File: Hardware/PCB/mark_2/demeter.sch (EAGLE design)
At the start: 70 parts, among them IC1 4050, IC2 LM1117-5.0, IC3 LM1117-3.3, IC4 M24C64, IC5 MCP3424, IC6 MCP23017SO, IC7 MAX485, IC8 ATMEGA32U4-AU, Q1 IRLML6402, Q2 IRLML6402, Q3 IRLML6402, Q4 IRLML6402, Q5 IRLML6402, Q6 IRLML6402, Q7 IRLML6402, Q8 IRLML6402

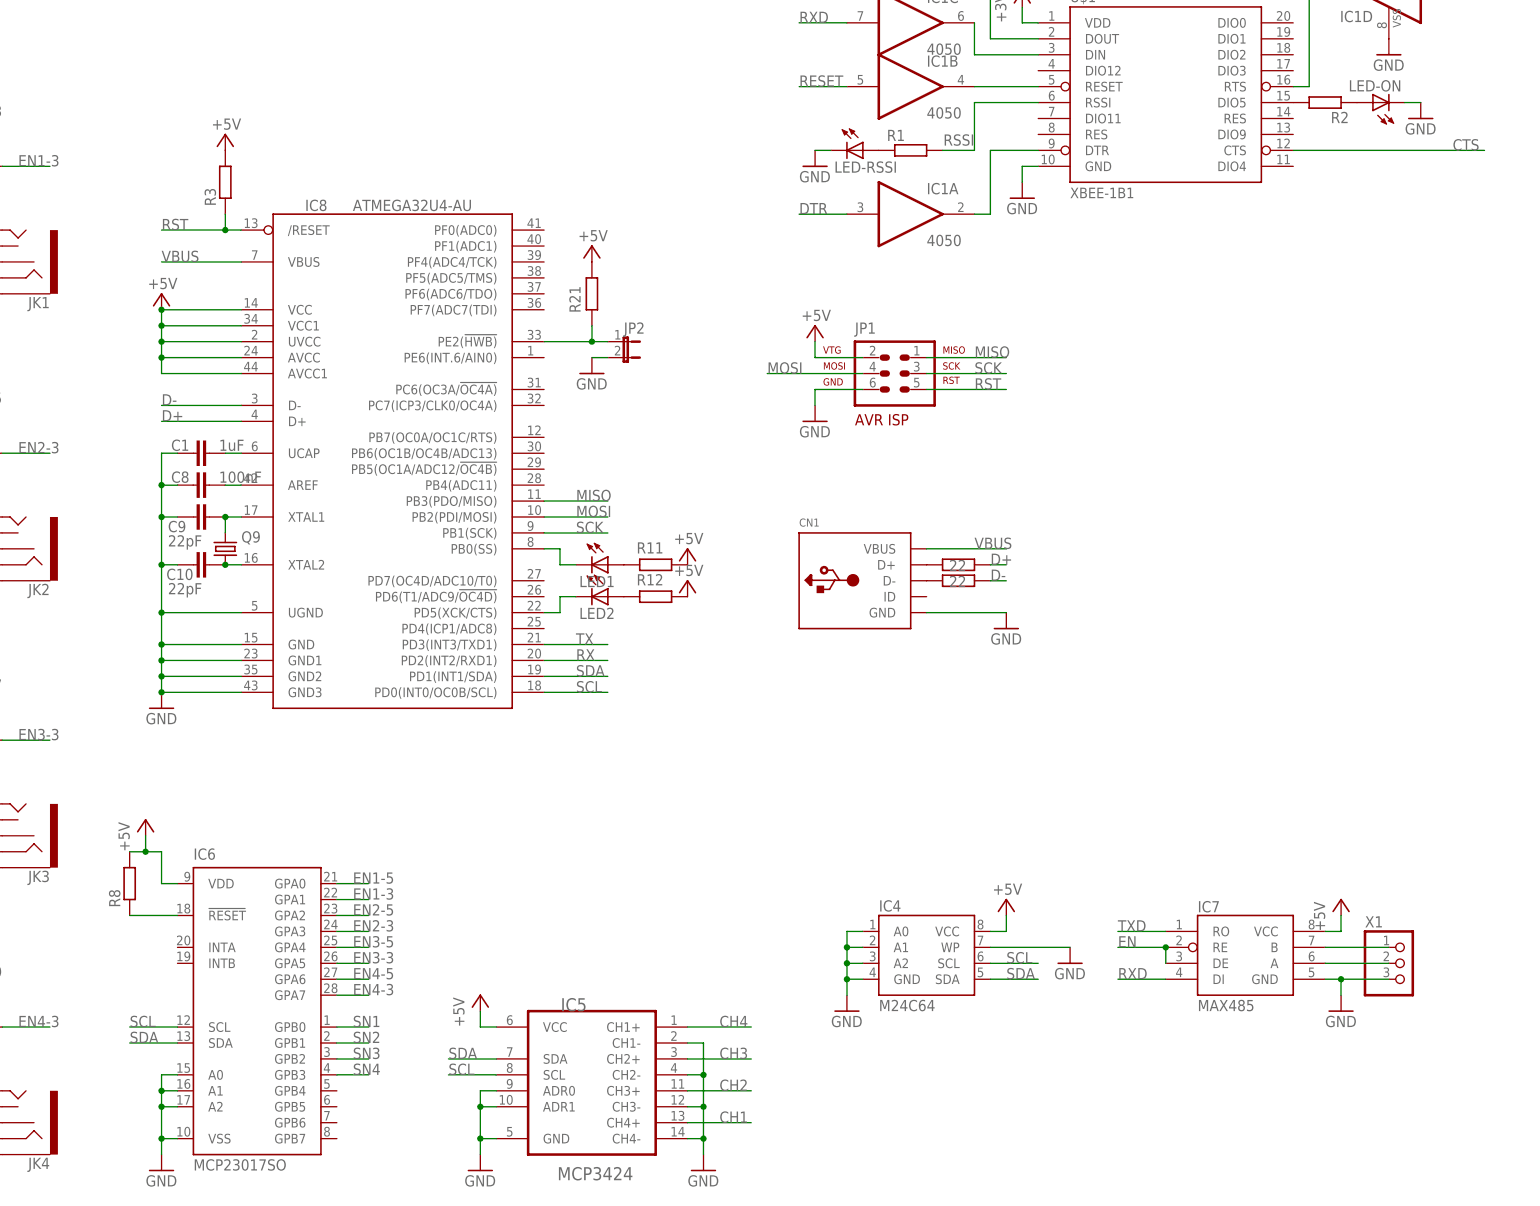
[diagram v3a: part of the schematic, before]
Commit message: 
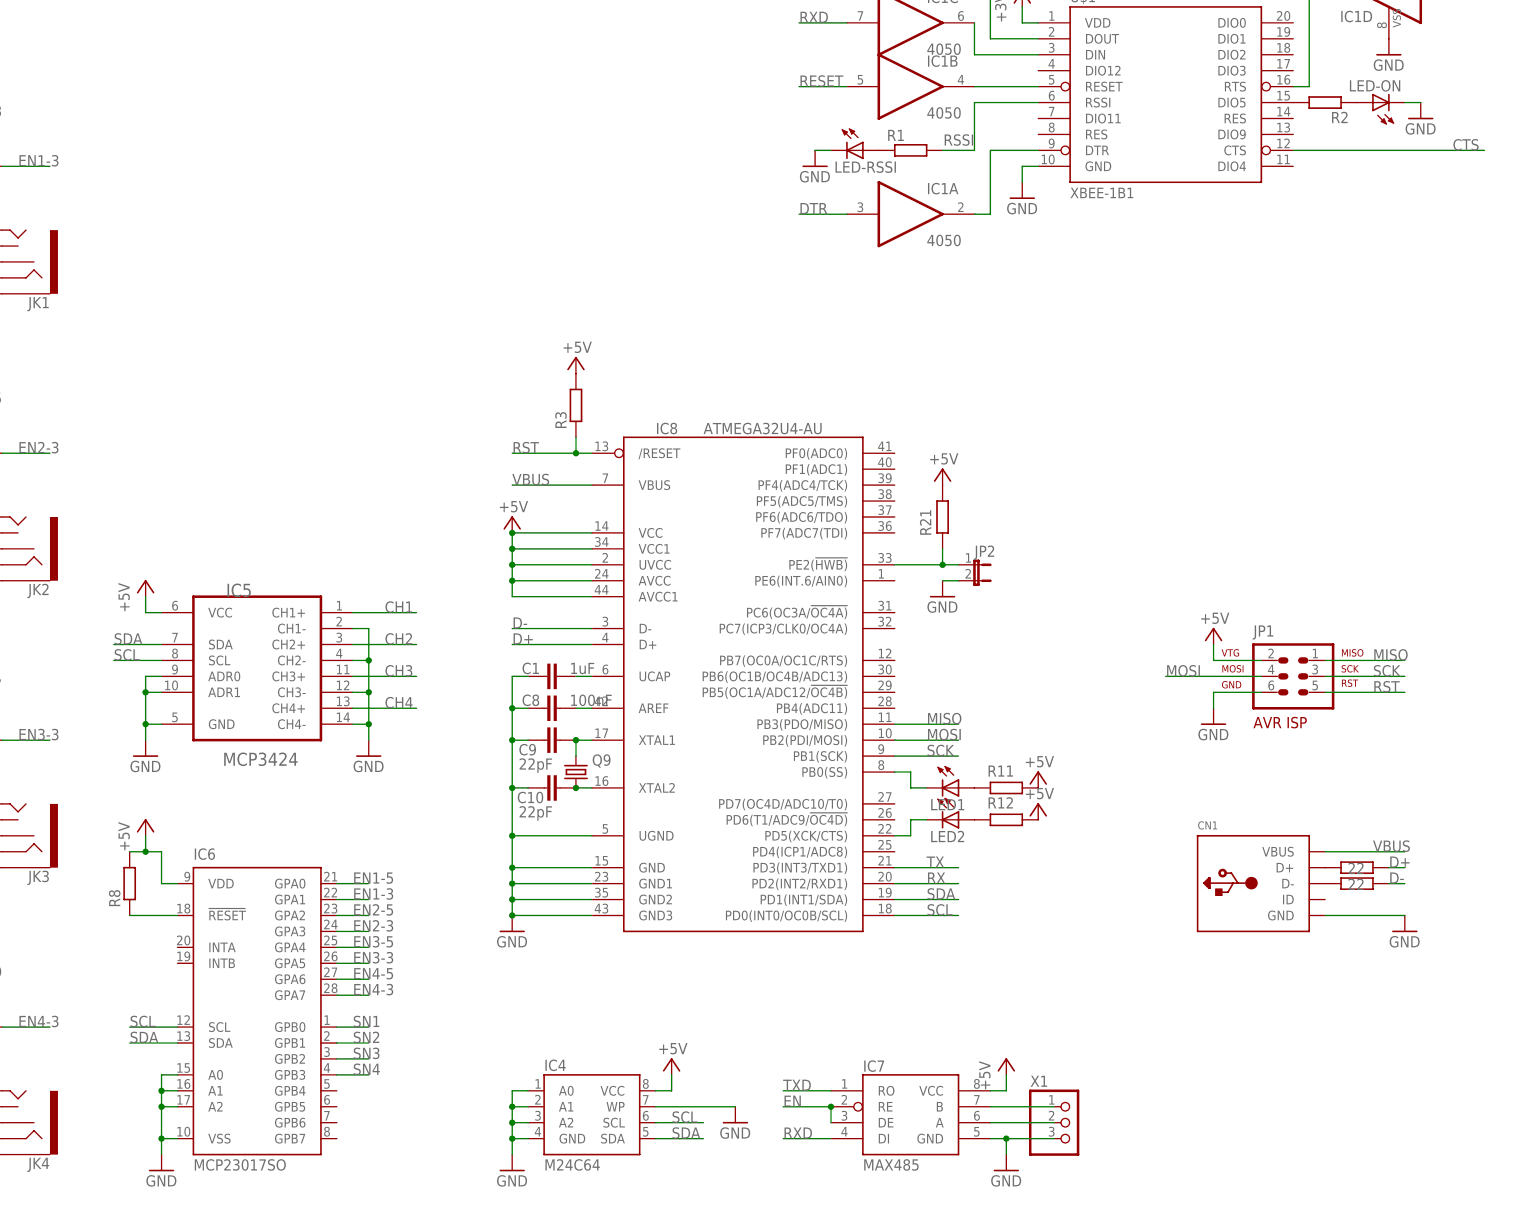
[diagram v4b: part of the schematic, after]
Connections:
- net CH1: now also IC5.CH1+; no longer IC5.CH4+
- net CH2: now also IC5.CH2+; no longer IC5.CH3+
- net CH3: now also IC5.CH3+; no longer IC5.CH2+
- net CH4: now also IC5.CH4+; no longer IC5.CH1+
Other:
- moved on the sheet: C1, C10, C8, C9, CN1, IC4, IC5, IC7, IC8, JP1, JP2, LED1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

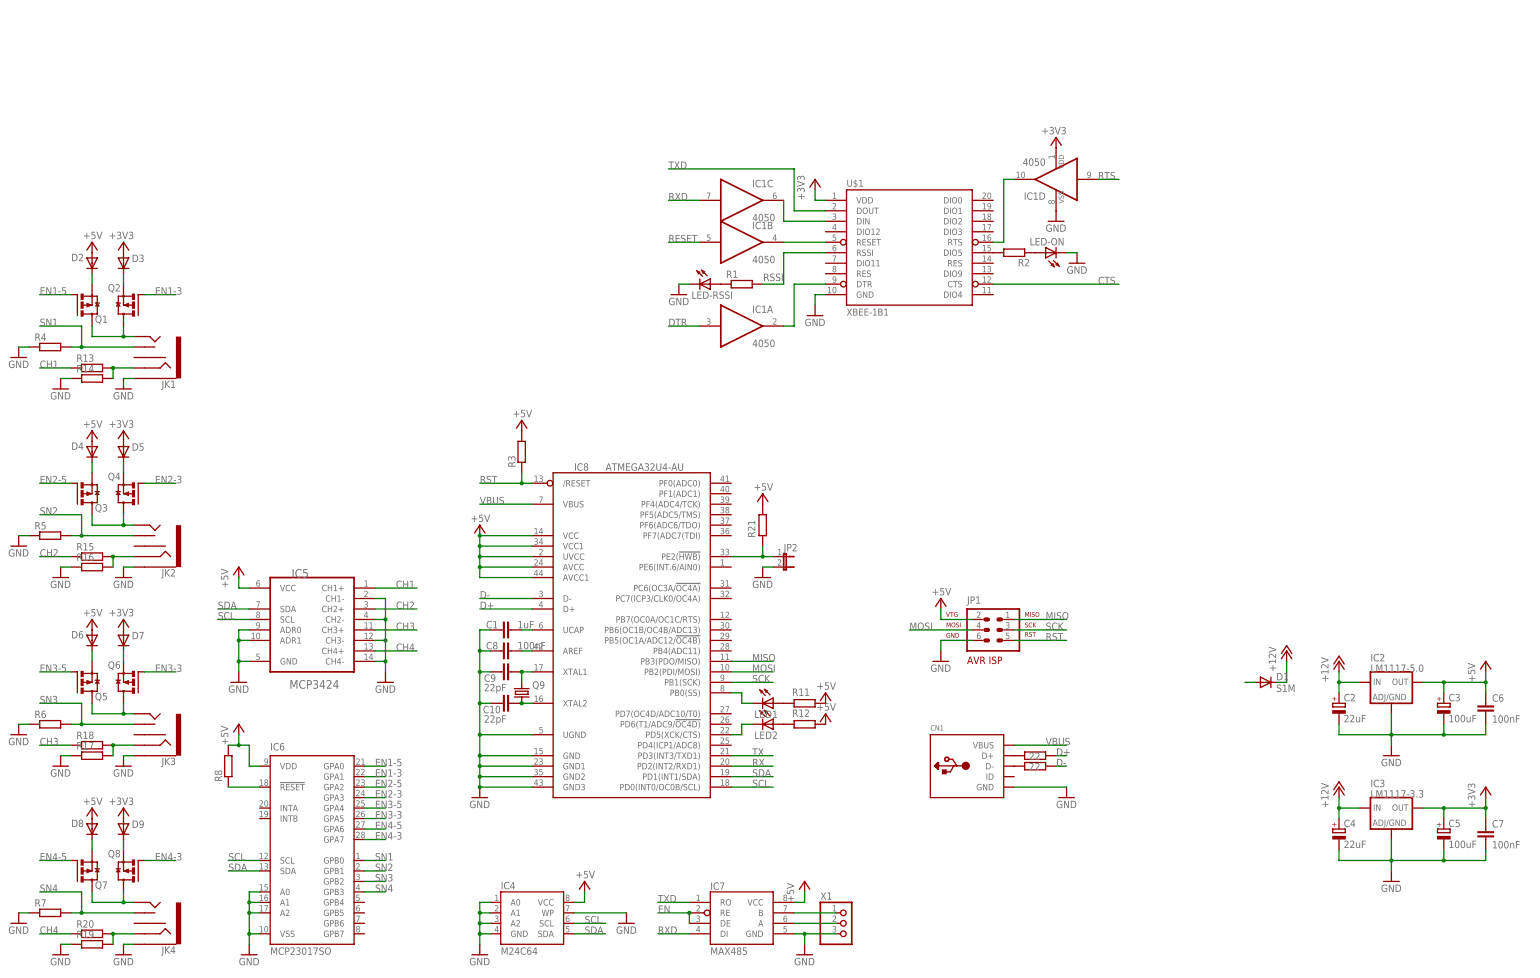
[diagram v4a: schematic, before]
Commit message: 
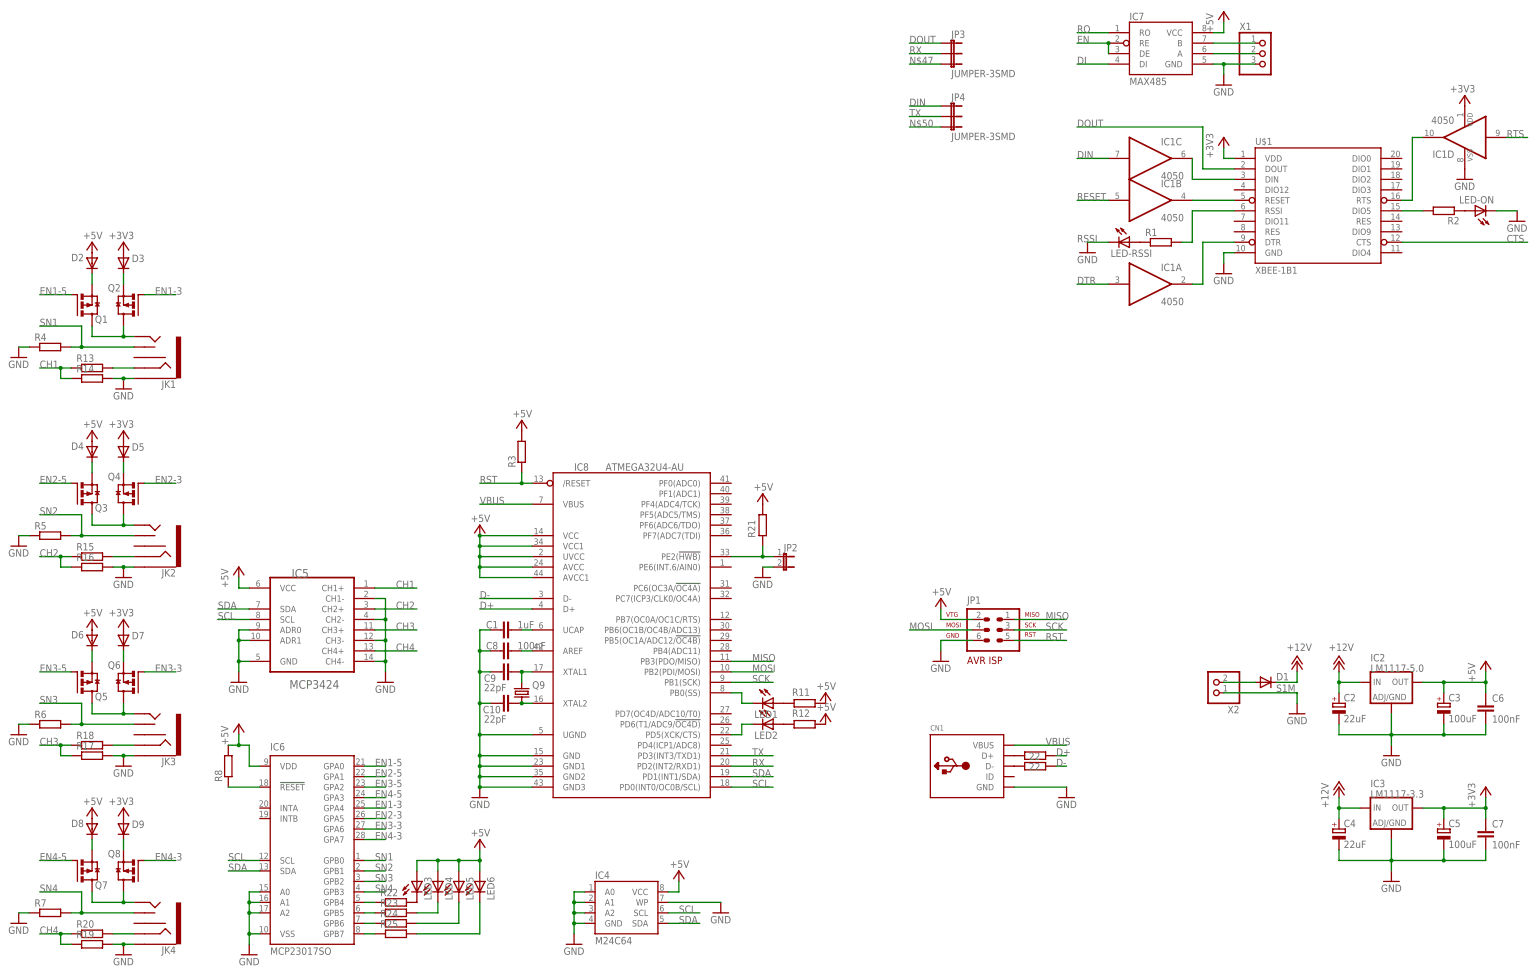
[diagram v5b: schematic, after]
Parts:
- added JP3, JP4: JUMPER-3SMD, mark_2:JUMPER-3SMD
- added LED3, LED4, LED5, LED6: (no value), mark_2:LED0805
- added R22, R23, R24, R25: (no value), mark_2:R-EU_R0805
- added X2: (no value), mark_2:W237-102
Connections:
- removed net RXD: IC1C.I, IC7.DI
- removed net TXD: IC7.RO, U$1.DOUT
- new net DI: IC7.DI
- new net DIN: IC1C.I, JP4.1
- new net DOUT: JP3.1, U$1.DOUT
- new net N$37: LED3.C, R22.2
- new net N$39: LED4.C, R23.2
- new net N$40: LED5.C, R24.2
- new net N$41: LED6.C, R25.2
- new net N$42: IC6.GPB7, R25.1
- new net N$43: IC6.GPB6, R24.1
- new net N$44: IC6.GPB5, R23.1
- new net N$45: IC6.GPB4, R22.1
- new net N$47: JP3.3
- new net N$50: JP4.3
- new net RO: IC7.RO
- net +5V: now also LED3.A, LED4.A, LED5.A, LED6.A
- net CH1: now also R14.1
- net CH2: now also R16.1
- net CH3: now also R17.1
- net CH4: now also R19.1
- net EN1-3: now also IC6.GPA4; no longer IC6.GPA1
- net EN2-3: now also IC6.GPA5; no longer IC6.GPA3
- net EN2-5: now also IC6.GPA1; no longer IC6.GPA2
- net EN3-3: now also IC6.GPA6; no longer IC6.GPA5
- net EN3-5: now also IC6.GPA2; no longer IC6.GPA4
- net EN4-5: now also IC6.GPA3; no longer IC6.GPA6
- net GND: now also R14.2, R16.2, R17.2, R19.2, X2.1; no longer R14.1, R16.1, R17.1, R19.1
- net N$1: now also X2.2
- net N$30: no longer R14.2
- net N$32: no longer R16.2
- net N$34: no longer R17.2
- net N$35: no longer R19.2
- net RX: now also JP3.2
- net TX: now also JP4.2
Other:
- moved on the sheet: IC1A, IC1B, IC1C, IC1D, IC4, IC7, LED-ON, LED-RSSI, R1, R2, U$1, X1
